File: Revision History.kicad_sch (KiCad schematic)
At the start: 0 parts

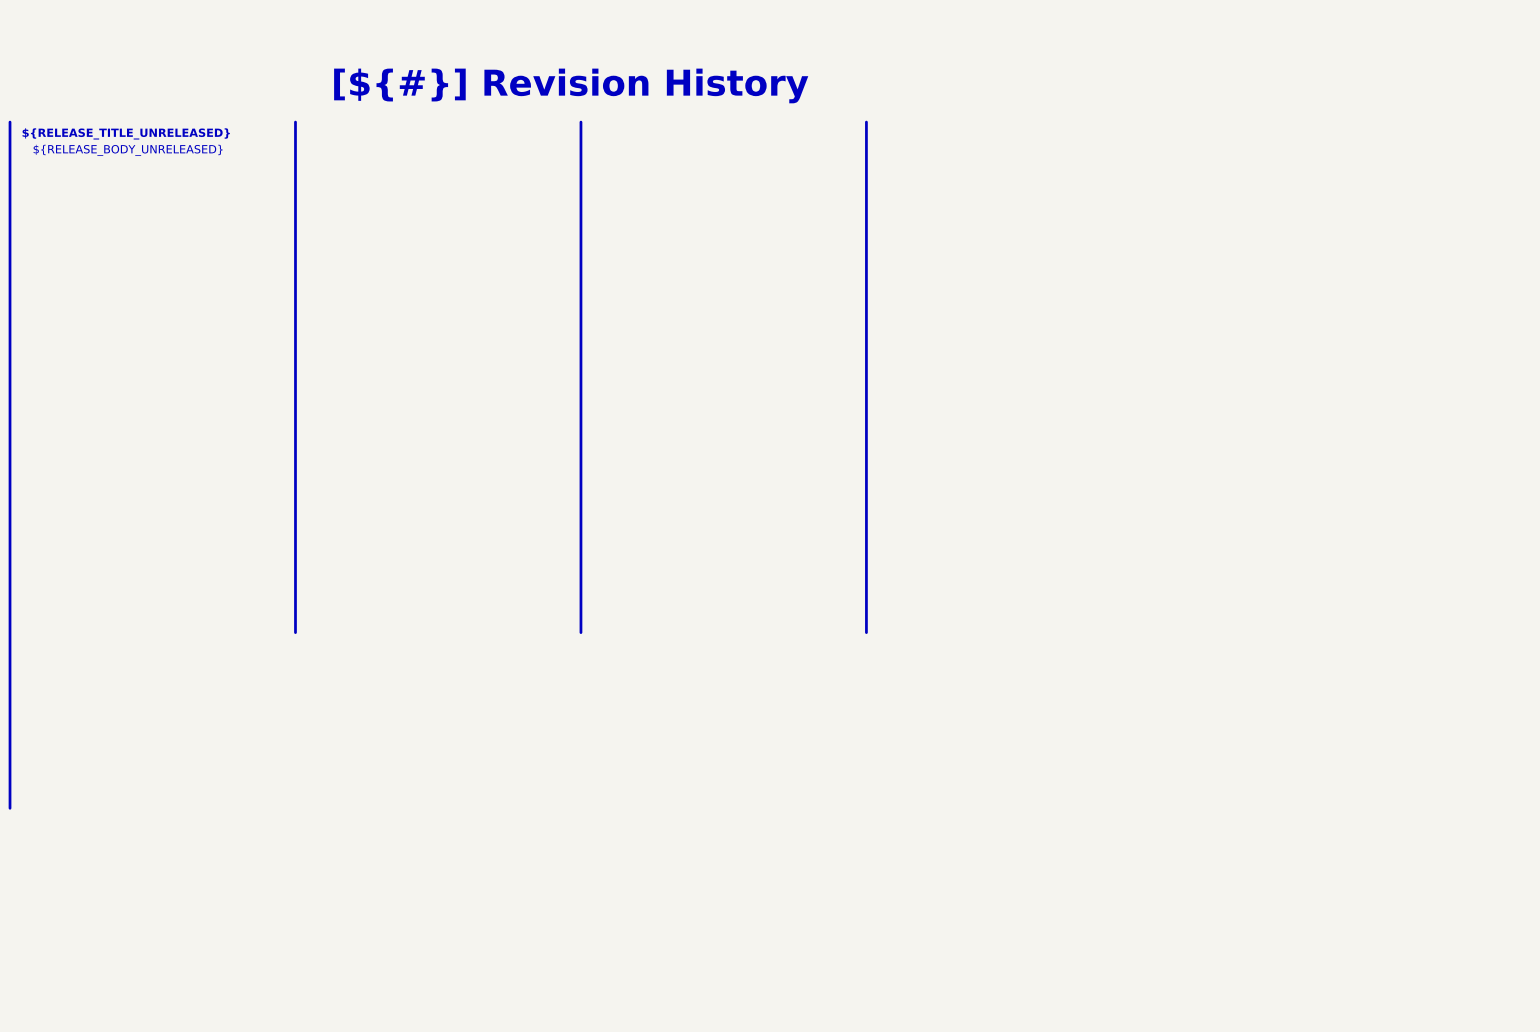
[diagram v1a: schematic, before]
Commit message: Restyle the schematic like OPEN_PHASE, merge the power sheets, rework the bottom silkscreen
- Schematic: all sheets on A3 in the OPEN_PHASE look (red header bands,
  DESCRIPTION / DESIGN NOTE / LAYOUT NOTE / CALCULS & BUDGET panels in
  French, TEST POINTS panel, References in the title block)
- Title block: INGENIERIE FRANCE logo in KDT_Template_GIT.kicad_wks,
  per-sheet logo images removed
- Power - Sequencing rebuilt with curves from LTspice simulations 01-04
- TPS61086 and LT3042 sheets merged into Power Supply - Analog Rails
  (page 5, keeps the TPS sheet UUID); pages renumbered to 9, local nets
  renamed to /Project Architecture/Power_Supply/*, PCB links updated
- PCB: per-rail net colours (+3.3V, +6V, +5VA, GND) as on OPEN_PHASE
- PCB B.SilkS: test point pills with Arial Black knockout names, J1
  pinout cells, E+/E-/S+/S- tags on the M12 pads, CELL 1 / CELL 2 titles
  and a LOAD CELL wiring panel

Netlist connectivity, ERC (2 warnings) and copper DRC unchanged;
schematic parity clean.

Co-Authored-By: Claude Opus 5.5 <noreply@anthropic.com>
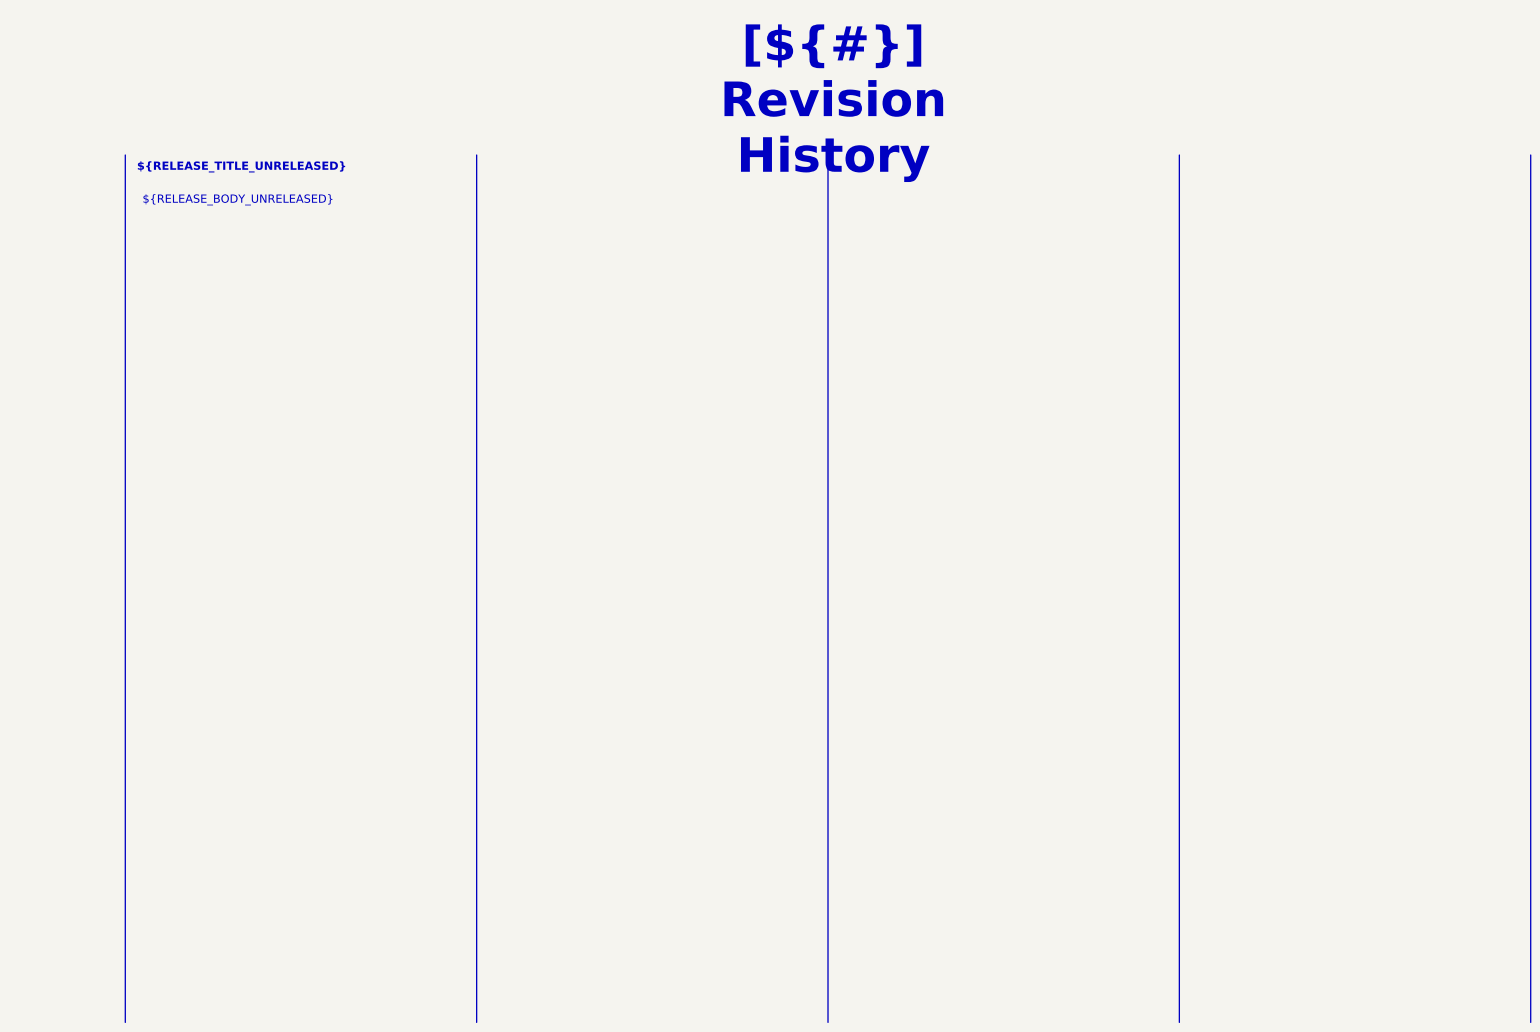
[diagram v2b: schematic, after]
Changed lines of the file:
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@@
 	(generator "eeschema")
 	(generator_version "10.0")
-	(paper "A4")
+	(paper "A3")
 	(title_block
 		(title "Revision History")
@@
 		(company "${COMPANY}")
 	)
-	(text_box ""
-		(exclude_from_sim no)
-		(at 220.98 35.56 0)
-		(size 58.42 111.76)
-		(margins 1.4287 1.4287 1.4287 1.4287)
-		(stroke
-			(width -0.0001)
-			(type default)
-		)
-		(fill
-			(type none)
-		)
-		(effects
-			(font
-				(face "Arial")
-				(size 1.905 1.905)
-				(color 0 0 0 1)
-			)
-			(justify left top)
-		)
-	)
 	(text_box "[${#}] ${TITLE}"
 		(exclude_from_sim no)
-		(at 80.01 16.51 0)
-		(size 137.16 12.7)
-		(margins 4.4999 4.4999 4.4999 4.4999)
+		(at 161.29 20.32 0)
+		(size 96.52 12.7)
+		(margins 5.9999 5.9999 5.9999 5.9999)
 		(stroke
 			(width -0.0001)
@@
 			(font
 				(face "Times New Roman")
-				(size 6 6)
+				(size 8 8)
 				(thickness 1.2)
 				(bold yes)
@@
 	(text_box "${RELEASE_BODY_UNRELEASED}"
 		(exclude_from_sim no)
-		(at 22.86 35.56 0)
-		(size 58.42 146.05)
-		(margins 1.4287 1.4287 1.4287 1.4287)
-		(stroke
-			(width -0.0001)
-			(type default)
-		)
-		(fill
-			(type none)
-		)
-		(effects
-			(font
-				(face "Arial")
-				(size 1.905 1.905)
-				(color 0 0 0 1)
-			)
-			(justify left top)
-		)
-	)
-	(text_box ""
-		(exclude_from_sim no)
-		(at 152.4 31.75 0)
-		(size 57.15 7.62)
-		(margins 1.4287 1.4287 1.4287 1.4287)
-		(stroke
-			(width -0.0001)
-			(type default)
-		)
-		(fill
-			(type none)
-		)
-		(effects
-			(font
-				(face "Arial")
-				(size 1.905 1.905)
-				(thickness 0.254)
-				(bold yes)
-			)
-			(justify left top)
-		)
-	)
-	(text_box ""
-		(exclude_from_sim no)
-		(at 154.94 35.56 0)
-		(size 58.42 111.76)
-		(margins 1.4287 1.4287 1.4287 1.4287)
-		(stroke
-			(width -0.0001)
-			(type default)
-		)
-		(fill
-			(type none)
-		)
-		(effects
-			(font
-				(face "Arial")
-				(size 1.905 1.905)
-				(color 0 0 0 1)
-			)
-			(justify left top)
-		)
-	)
-	(text_box ""
-		(exclude_from_sim no)
-		(at 88.9 35.56 0)
-		(size 57.15 105.41)
+		(at 48.26 46.99 0)
+		(size 76.2 191.77)
 		(margins 1.4287 1.4287 1.4287 1.4287)
 		(stroke
@@
 	(text_box "${RELEASE_TITLE_UNRELEASED}"
 		(exclude_from_sim no)
-		(at 20.32 31.75 0)
-		(size 57.15 7.62)
+		(at 46.99 39.37 0)
+		(size 78.74 6.35)
 		(margins 1.4287 1.4287 1.4287 1.4287)
 		(stroke
@@
 		)
 		(fill
-			(type none)
+			(type color)
+			(color 162 22 34 1)
 		)
 		(effects
@@
 				(thickness 0.254)
 				(bold yes)
-			)
-			(justify left top)
-		)
-	)
-	(text_box ""
-		(exclude_from_sim no)
-		(at 86.36 31.75 0)
-		(size 57.15 7.62)
-		(margins 1.4287 1.4287 1.4287 1.4287)
-		(stroke
-			(width -0.0001)
-			(type default)
-		)
-		(fill
-			(type none)
-		)
-		(effects
-			(font
-				(face "Arial")
-				(size 1.905 1.905)
-				(thickness 0.254)
-				(bold yes)
-			)
-			(justify left top)
-		)
-	)
-	(text_box ""
-		(exclude_from_sim no)
-		(at 218.44 31.75 0)
-		(size 57.15 7.62)
-		(margins 1.4287 1.4287 1.4287 1.4287)
-		(stroke
-			(width -0.0001)
-			(type default)
-		)
-		(fill
-			(type none)
-		)
-		(effects
-			(font
-				(face "Arial")
-				(size 1.905 1.905)
-				(thickness 0.254)
-				(bold yes)
+				(color 255 255 255 1)
 			)
 			(justify left top)
@@
 	(polyline
 		(pts
-			(xy 85.09 31.75) (xy 85.09 149.86)
+			(xy 289.56 39.37) (xy 289.56 240.03)
 		)
 		(stroke
-			(width 0.635)
-			(type default)
-			(color 0 0 0 1)
+			(width 0.3)
+			(type solid)
+			(color 190 190 190 1)
 		)
 	)
 	(polyline
 		(pts
-			(xy 151.13 31.75) (xy 151.13 149.86)
+			(xy 208.28 39.37) (xy 208.28 240.03)
 		)
 		(stroke
-			(width 0.635)
-			(type default)
-			(color 0 0 0 1)
+			(width 0.3)
+			(type solid)
+			(color 190 190 190 1)
 		)
 	)
 	(polyline
 		(pts
-			(xy 19.05 31.75) (xy 19.05 190.5)
+			(xy 370.84 39.37) (xy 370.84 240.03)
 		)
 		(stroke
-			(width 0.635)
-			(type default)
-			(color 0 0 0 1)
+			(width 0.3)
+			(type solid)
+			(color 190 190 190 1)
 		)
 	)
 	(polyline
 		(pts
-			(xy 217.17 31.75) (xy 217.17 149.86)
+			(xy 45.72 39.37) (xy 45.72 240.03)
 		)
 		(stroke
-			(width 0.635)
-			(type default)
-			(color 0 0 0 1)
+			(width 0.3)
+			(type solid)
+			(color 190 190 190 1)
 		)
 	)
+	(polyline
+		(pts
+			(xy 127 39.37) (xy 127 240.03)
+		)
+		(stroke
+			(width 0.3)
+			(type solid)
+			(color 190 190 190 1)
+		)
+	)
